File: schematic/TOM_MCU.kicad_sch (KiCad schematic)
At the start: 236 parts, among them J1 22053041, J10 Conn_01x02, J11 Conn_01x02, J2 22053041, J3 USB4216-03-A, J4 USB4216-03-A, J5 E1E2-Emulator-Interface, J6 EMU CFG, J7 UPSEL_CFG, J8 Conn_01x02, J9 Conn_01x02, SW1 OP_CFG, U1 TVS2200DRV, U10 DS18B20+, U2 TVS2200DRV, U3 LDL1117S33R, U4 CY7C65213A-28PVXI, U5 TPS2116DRLR, U6 TXS0102DCUT, U7 TXS0102DCUT, U8 MIC5205-2.5YM5-TR, U9 R5F572NNHGFP-30, Y1 ECS-240-8-30B-CKM-TR

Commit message: TOM_MCU PCB
I think that we can remove Priority Switchover unless we wanted to add the 3v3 buck test pin into it. Or remove it and have BUS_3V3 be the board 3v3. Plus I left the other pins currently disconnected on the R5F5, but left the labels there currently, for if we wanted to add more test points.
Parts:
- removed TP15, TP16, TP17, TP18, TP19, TP20, TP21, TP22, TP23, TP24, TP25, TP26, TP27, TP28, TP29, TP30, TP31, TP32, TP33, TP34, TP35, TP36, TP37, TP38, TP39, TP40, TP41, TP42, TP43, TP44, TP45, TP46, TP47, TP48, TP49, TP50, TP51, TP52, TP53, TP54, TP55, TP56, TP57, TP58, TP59, TP60, TP61, TP62, TP63, TP64, TP65, TP66, TP67, TP68, TP69, TP70, TP71, TP72, TP73, TP74: 3825, 3825, symbol 3825:3825
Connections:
- net BMS_I2C_CLK: no longer TP10.1
- net BMS_I2C_DATA: no longer TP11.1
- net BMS_SMBUS_CLK: now also TP13.1
- net BMS_SMBUS_DATA: now also TP12.1
- net BOARD_3V3: no longer TP2.1
- net DBG_RESETn: now also TP6.1
- net DSW_MD_FINED: now also TP3.1
- net EMU_EMLE: now also TP2.1
- net EMU_TCK: now also TP9.1
- net EMU_TMS: now also TP8.1
- net EMU_TRSTn: now also TP7.1
- net ENCODER0_PHASE_A: no longer TP7.1
- net ENCODER0_PHASE_B: no longer TP13.1
- net ENCODER1_PHASE_A: no longer TP14.1
- net ENCODER1_PHASE_B: no longer TP9.1
- net ENCODER3_PHASE_A: no longer TP6.1
- net GND: now also TP14.1
- net PMOD_JC_SCL: now also TP11.1
- net PMOD_JC_SDA: now also TP10.1
- net RSPIC_MOTOR0_nCS: no longer TP12.1
- net RSPIC_MOTOR1_nCS: no longer TP8.1
- net RSPIC_MOTOR2_nCS: no longer TP3.1
- net SCI_USBC_VBUS: now reaches C10.2, C11.2, C8.2, C9.2, FB2.1, J4.A4 (VBUS_1), J4.B4 (VBUS_2), U2.4 (IN), U2.5 (IN), U2.6 (IN)
- net USB0_VBUS: now reaches C1.2, C2.2, C3.2, C4.2, FB1.1, J3.A4 (VBUS_1), J3.B4 (VBUS_2), U1.4 (IN), U1.5 (IN), U1.6 (IN)

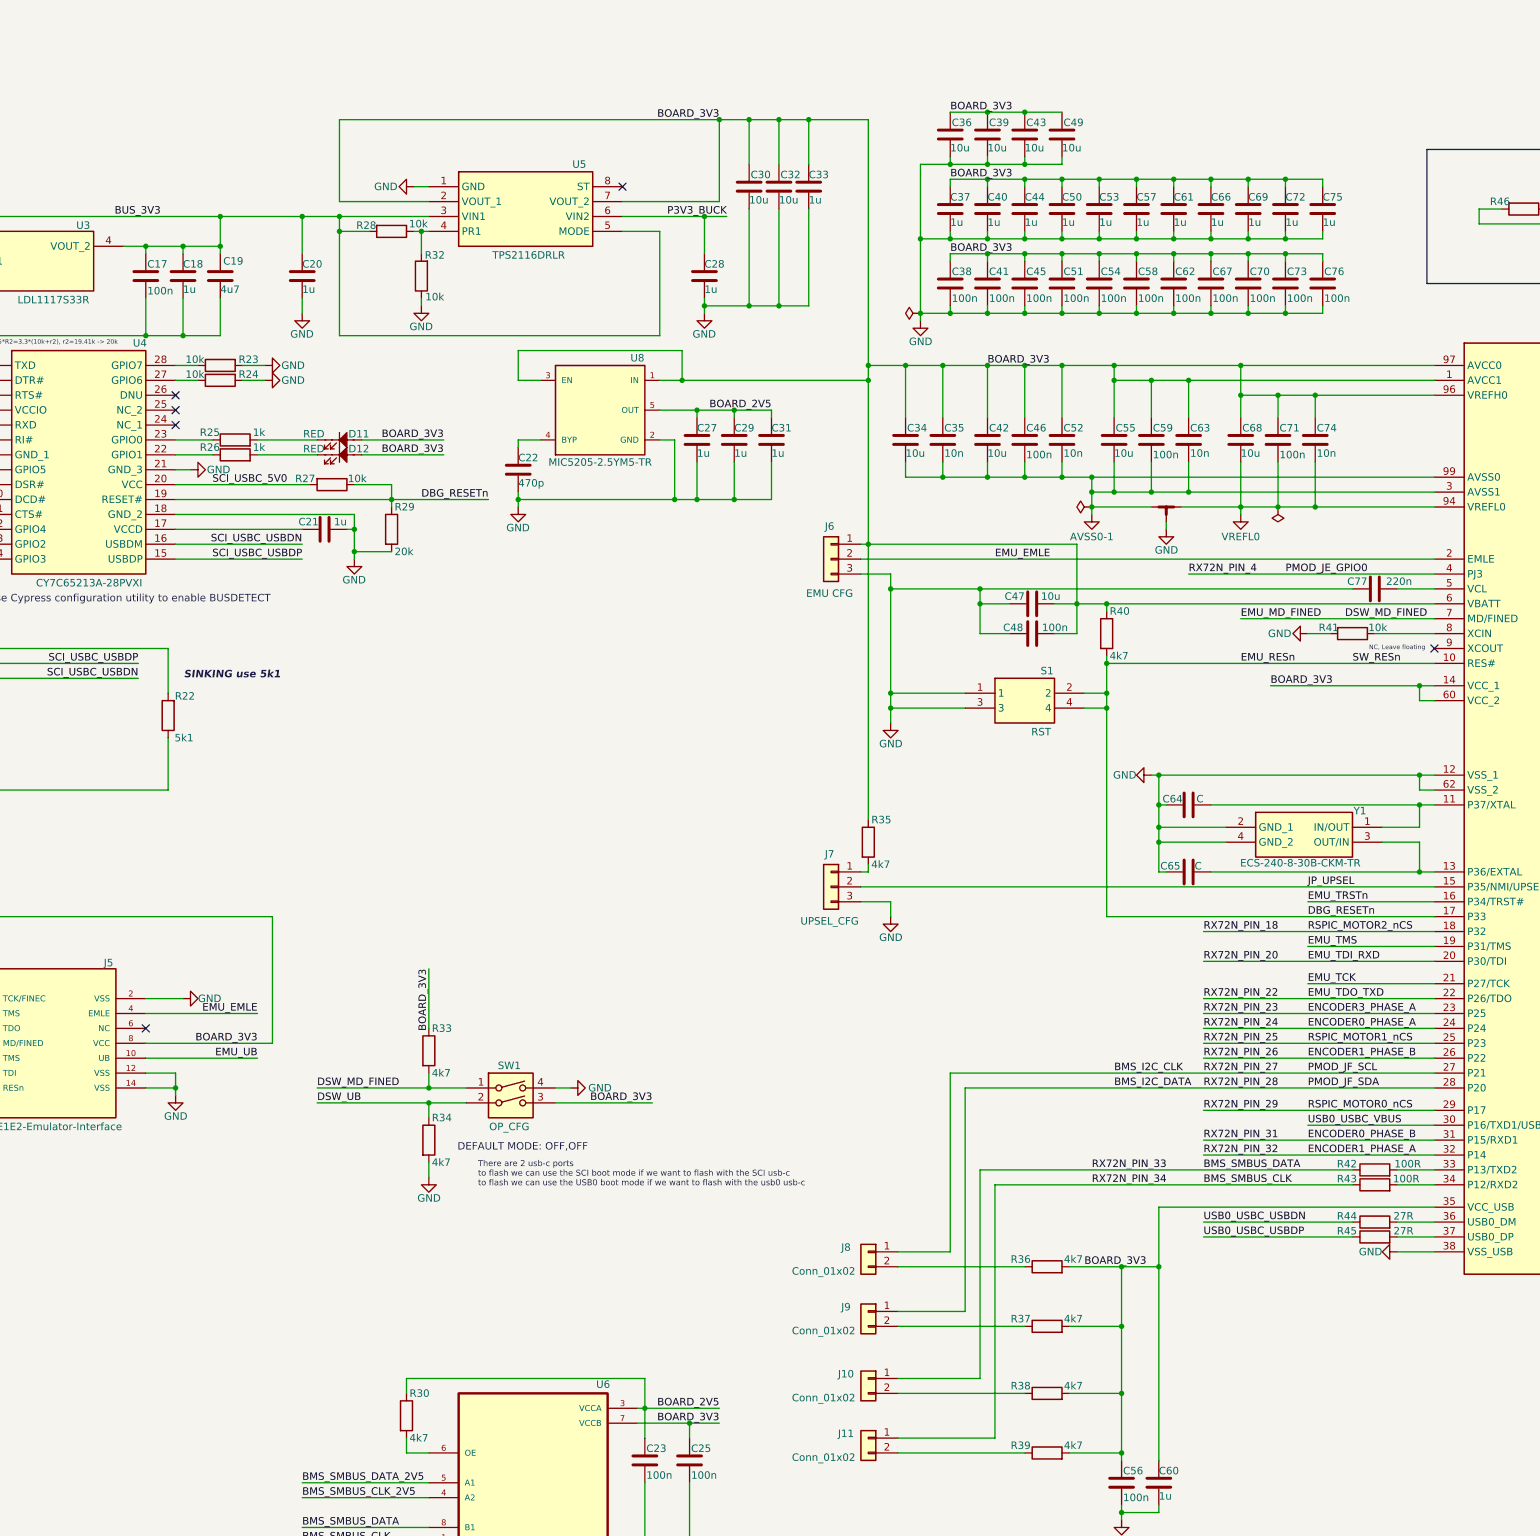
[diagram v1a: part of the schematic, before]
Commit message: Redo after Review #1
Double check USBC Data lines should be within spec.
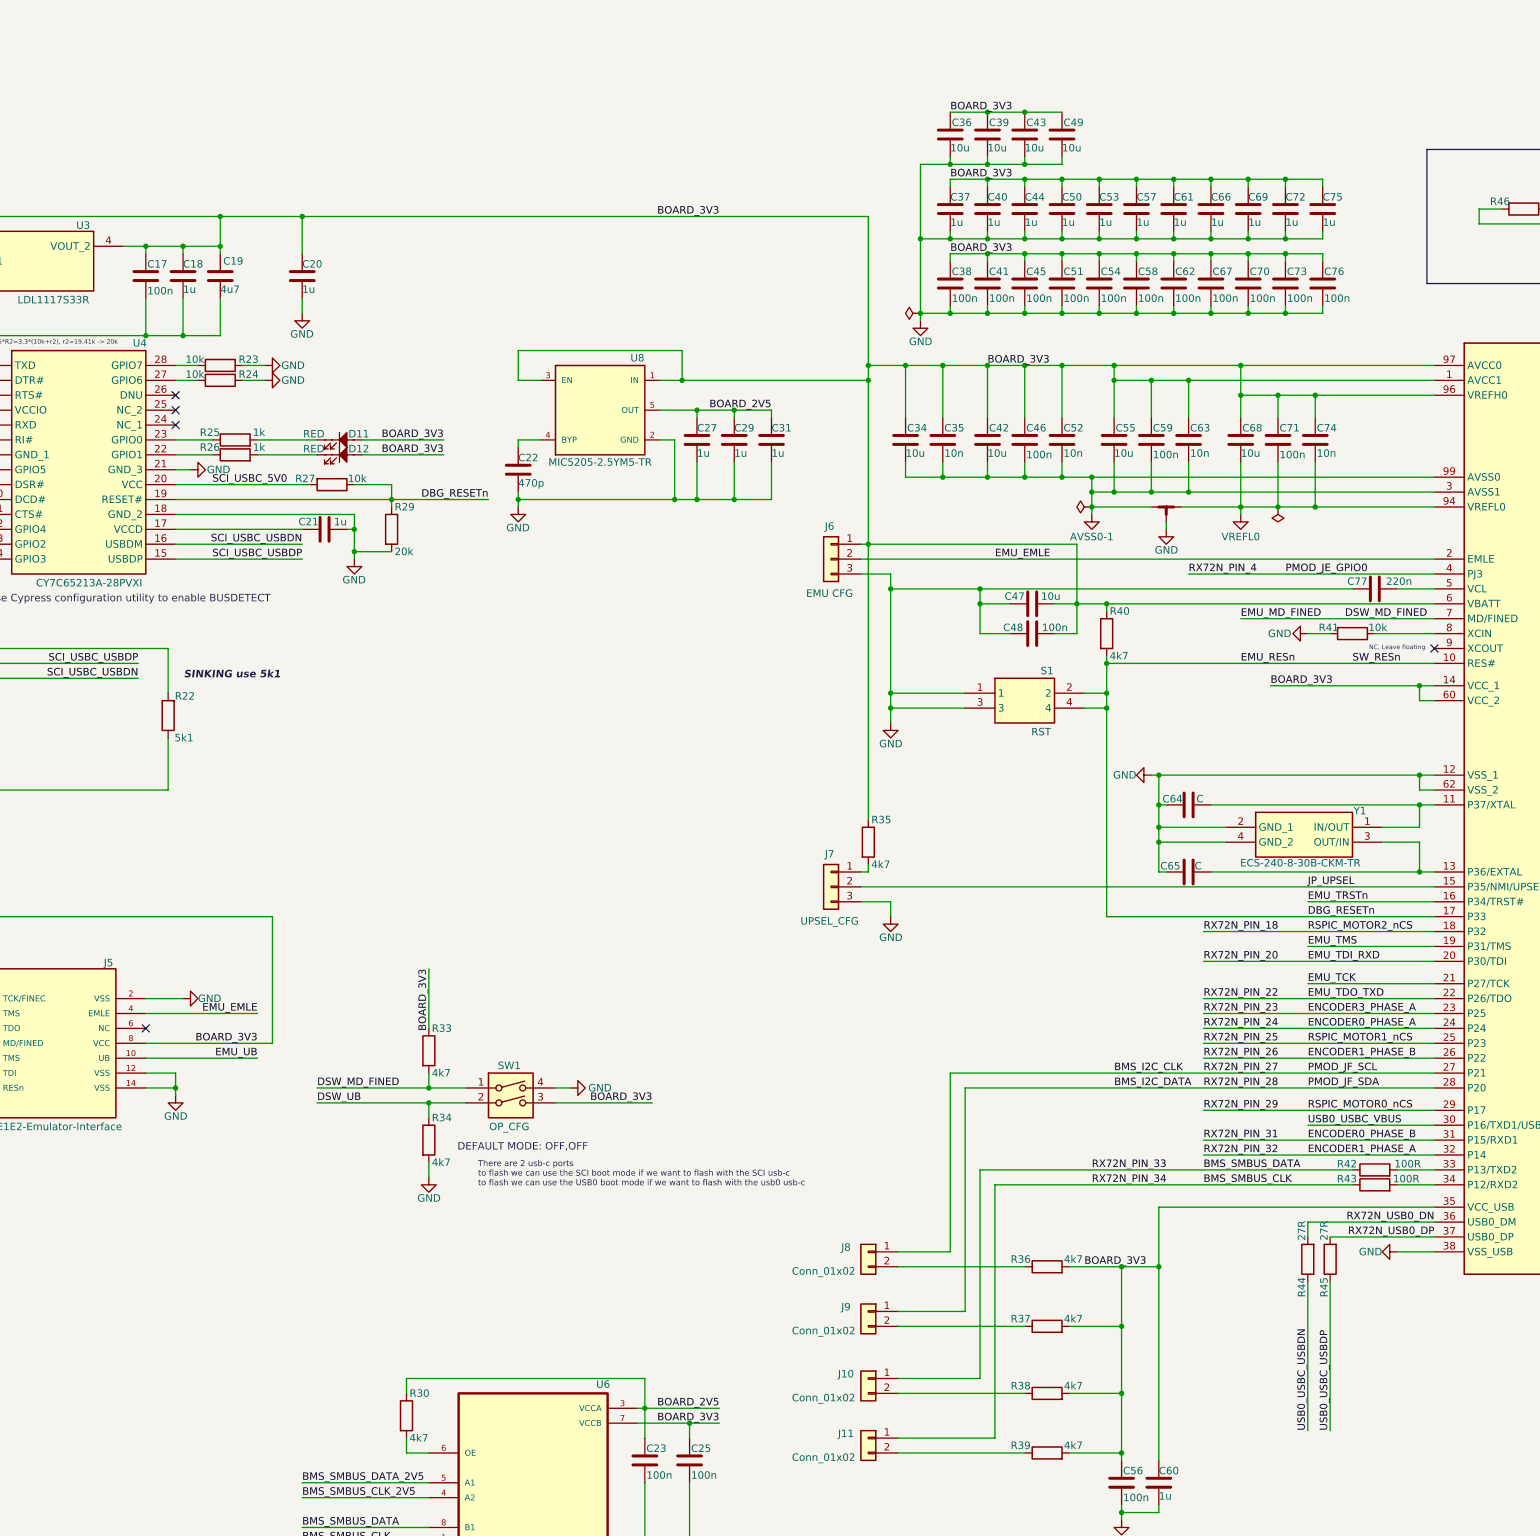
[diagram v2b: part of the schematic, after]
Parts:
- removed C28, C33: 1u, Capacitor_SMD:C_0603_1608Metric_Pad1.08x0.95mm_HandSolder, symbol Device:C
- removed C30, C32: 10u, Capacitor_SMD:C_0805_2012Metric_Pad1.18x1.45mm_HandSolder, symbol Device:C
- removed R28, R32: 10k, Resistor_SMD:R_0603_1608Metric_Pad0.98x0.95mm_HandSolder, symbol Device:R
- removed U5: TPS2116DRLR, TPS2116DRLR:TPS62932DRLR, symbol TPS2116DRLR:TPS2116DRLR
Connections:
- net BUS_3V3 is gone; now on net BOARD_3V3: C17.1, C18.1, C19.1, C20.1, U3.2 (VOUT_1), U3.4 (VOUT_2)
- net RX72N_USB0_DP: now reaches R45.2, U9.37 (USB0_DP)
- net RX72N_USB0_DN: now reaches R44.2, U9.36 (USB0_DM)
- no-connect marks 16 -> 15
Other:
- moved on the sheet: R44, R45

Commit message: Fixed everything from last push
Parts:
- added TP15, TP16, TP17, TP18: 3825, 3825, symbol 3825:3825
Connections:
- net BMS_I2C_CLK: now also TP15.1
- net BMS_I2C_DATA: now also TP16.1
- net DS18B20_DQ: no longer U9.100 (P05)
- net PMOD_JD_GPIO0: no longer U9.79 (PD7)
- net PMOD_JD_GPIO1: no longer U9.80 (PD6)
- net PMOD_JD_GPIO2: no longer U9.81 (PD5)
- net PMOD_JD_GPIO3: no longer U9.82 (PD4)
- net RX72N_PIN_53: now also TP18.1
- net RX72N_PIN_54: now also TP17.1
- net ENCODER0_PHASE_A: no longer names the net of U9.24 (P24)
- net ENCODER0_PHASE_B: no longer names the net of U9.31 (P15/RXD1)
- net ENCODER1_PHASE_A: no longer names the net of U9.32 (P14)
- net ENCODER1_PHASE_B: no longer names the net of U9.26 (P22)
- net ENCODER2_PHASE_A: no longer names the net of U9.51 (PC1)
- net ENCODER2_PHASE_B: no longer names the net of U9.52 (PC0)
- net ENCODER3_PHASE_A: no longer names the net of U9.23 (P25)
- net ENCODER3_PHASE_B: no longer names the net of U9.67 (PA3)
- net MOTOR0_EN: no longer names the net of U9.76 (PE2)
- net MOTOR0_IPROPI: no longer names the net of U9.95 (P40)
- net MOTOR0_PH: no longer names the net of U9.73 (PE5)
- net MOTOR0_nFAULT: no longer names the net of U9.90 (P44)
- net MOTOR1_EN: no longer names the net of U9.77 (PE1)
- net MOTOR1_IPROPI: no longer names the net of U9.93 (P41)
- net MOTOR1_PH: no longer names the net of U9.74 (PE4)
- net MOTOR1_nFAULT: no longer names the net of U9.89 (P45)
- net MOTOR2_EN: no longer names the net of U9.78 (PE0)
- net MOTOR2_IPROPI: no longer names the net of U9.92 (P42)
- net MOTOR2_PH: no longer names the net of U9.75 (PE3)
- net MOTOR2_nFAULT: no longer names the net of U9.88 (P46)
- net MOTOR3_EN: no longer names the net of U9.72 (PE6)
- net MOTOR3_IPROPI: no longer names the net of U9.91 (P43)
- net MOTOR3_PH: no longer names the net of U9.71 (PE7)
- net MOTOR3_nFAULT: no longer names the net of U9.87 (P47)
- net PMOD_JA_CIPO: no longer names the net of U9.43 (P51)
- net PMOD_JA_COPI: no longer names the net of U9.44 (P50)
- net PMOD_JA_CS0: no longer names the net of U9.42 (P52)
- net PMOD_JA_CS1: no longer names the net of U9.55 (PB5)
- net PMOD_JA_DC: no longer names the net of U9.56 (PB4)
- net PMOD_JA_GPIO: no longer names the net of U9.58 (PB2)
- net PMOD_JA_RST: no longer names the net of U9.57 (PB3)
- net PMOD_JA_SCK: no longer names the net of U9.41 (P53)
- net PMOD_JB_GPIO0: no longer names the net of U9.46 (PC6)
- net PMOD_JB_GPIO1: no longer names the net of U9.39 (P55)
- net PMOD_JB_GPIO2: no longer names the net of U9.40 (P54)
- net PMOD_JB_GPIO3: no longer names the net of U9.68 (PA2)
- net PMOD_JC_INT1: no longer names the net of U9.48 (PC4)
- net PMOD_JC_INT2: no longer names the net of U9.47 (PC5)
- net PMOD_JE_GPIO1: no longer names the net of U9.59 (PB1)
- net PMOD_JE_GPIO2: no longer names the net of U9.61 (PB0)
- net PMOD_JE_GPIO3: no longer names the net of U9.69 (PA1)
- net PMOD_JF_GPIO0: no longer names the net of U9.86 (PD0)
- net PMOD_JF_GPIO1: no longer names the net of U9.98 (P07)
- net RPI5_RSPIA_CIPO: no longer names the net of U9.63 (PA7)
- net RPI5_RSPIA_COPI: no longer names the net of U9.64 (PA6)
- net RPI5_RSPIA_CS: no longer names the net of U9.66 (PA4)
- net RPI5_RSPIA_SCLK: no longer names the net of U9.65 (PA5)
- net RSPIC_CIPO: no longer names the net of U9.84 (PD2)
- net RSPIC_COPI: no longer names the net of U9.85 (PD1)
- net RSPIC_MOTOR0_nCS: no longer names the net of U9.29 (P17)
- net RSPIC_MOTOR1_nCS: no longer names the net of U9.25 (P23)
- net RSPIC_MOTOR2_nCS: no longer names the net of U9.18 (P32)
- net RSPIC_MOTOR3_nCS: no longer names the net of U9.70 (PA0)
- net RSPIC_SCLK: no longer names the net of U9.83 (PD3)
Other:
- moved on the sheet: TP14

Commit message: fixed tom
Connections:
- net DS18B20_DQ: now also U9.100 (P05)
- net PMOD_JD_GPIO0: now also U9.79 (PD7)
- net PMOD_JD_GPIO1: now also U9.80 (PD6)
- net PMOD_JD_GPIO2: now also U9.81 (PD5)
- net PMOD_JD_GPIO3: now also U9.82 (PD4)
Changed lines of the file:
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@@
 	(wire
 		(pts
+			(xy 787.4 128.27) (xy 762 128.27)
+		)
+		(stroke
+			(width 0)
+			(type default)
+		)
+	)
+	(wire
+		(pts
 			(xy 332.74 77.47) (xy 335.28 77.47)
 		)
@@
 	(wire
 		(pts
+			(xy 787.4 88.9) (xy 762 88.9)
+		)
+		(stroke
+			(width 0)
+			(type default)
+		)
+	)
+	(wire
+		(pts
 			(xy 265.43 77.47) (xy 299.72 77.47)
 		)
@@
 	(wire
 		(pts
+			(xy 787.4 130.81) (xy 762 130.81)
+		)
+		(stroke
+			(width 0)
+			(type default)
+		)
+	)
+	(wire
+		(pts
 			(xy 397.51 116.84) (xy 401.32 116.84)
 		)
@@
 	(wire
 		(pts
+			(xy 787.4 125.73) (xy 762 125.73)
+		)
+		(stroke
+			(width 0)
+			(type default)
+		)
+	)
+	(wire
+		(pts
 			(xy 631.19 88.9) (xy 637.54 88.9)
 		)
@@
 	(wire
 		(pts
+			(xy 787.4 133.35) (xy 762 133.35)
+		)
+		(stroke
+			(width 0)
+			(type default)
+		)
+	)
+	(wire
+		(pts
 			(xy 469.9 149.86) (xy 469.9 158.75)
 		)
@@
 		)
 	)
+	(label "PMOD_JD_GPIO2"
+		(at 787.4 128.27 180)
+		(effects
+			(font
+				(size 1.27 1.27)
+			)
+			(justify right bottom)
+		)
+	)
 	(label "BMS_I2C_DATA"
 		(at 54.61 119.38 0)
@@
 		)
 	)
+	(label "PMOD_JD_GPIO0"
+		(at 787.4 133.35 180)
+		(effects
+			(font
+				(size 1.27 1.27)
+			)
+			(justify right bottom)
+		)
+	)
 	(label "DS18B20_DQ"
 		(at 723.9 59.69 180)
@@
 		)
 	)
+	(label "PMOD_JD_GPIO1"
+		(at 787.4 130.81 180)
+		(effects
+			(font
+				(size 1.27 1.27)
+			)
+			(justify right bottom)
+		)
+	)
 	(label "DBG_RESETn"
 		(at 664.21 180.34 0)
@@
 		)
 	)
+	(label "PMOD_JD_GPIO3"
+		(at 787.4 125.73 180)
+		(effects
+			(font
+				(size 1.27 1.27)
+			)
+			(justify right bottom)
+		)
+	)
 	(label "SCI9_TXD9"
 		(at 793.75 198.12 180)
@@
 		(effects
 			(font
+				(size 1.27 1.27)
+			)
+			(justify right bottom)
+		)
+	)
+	(label "DS18B20_DQ"
+		(at 787.4 88.9 180)
+		(effects
+			(font
